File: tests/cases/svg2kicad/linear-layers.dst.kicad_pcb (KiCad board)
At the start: 2 copper layers, 0 parts

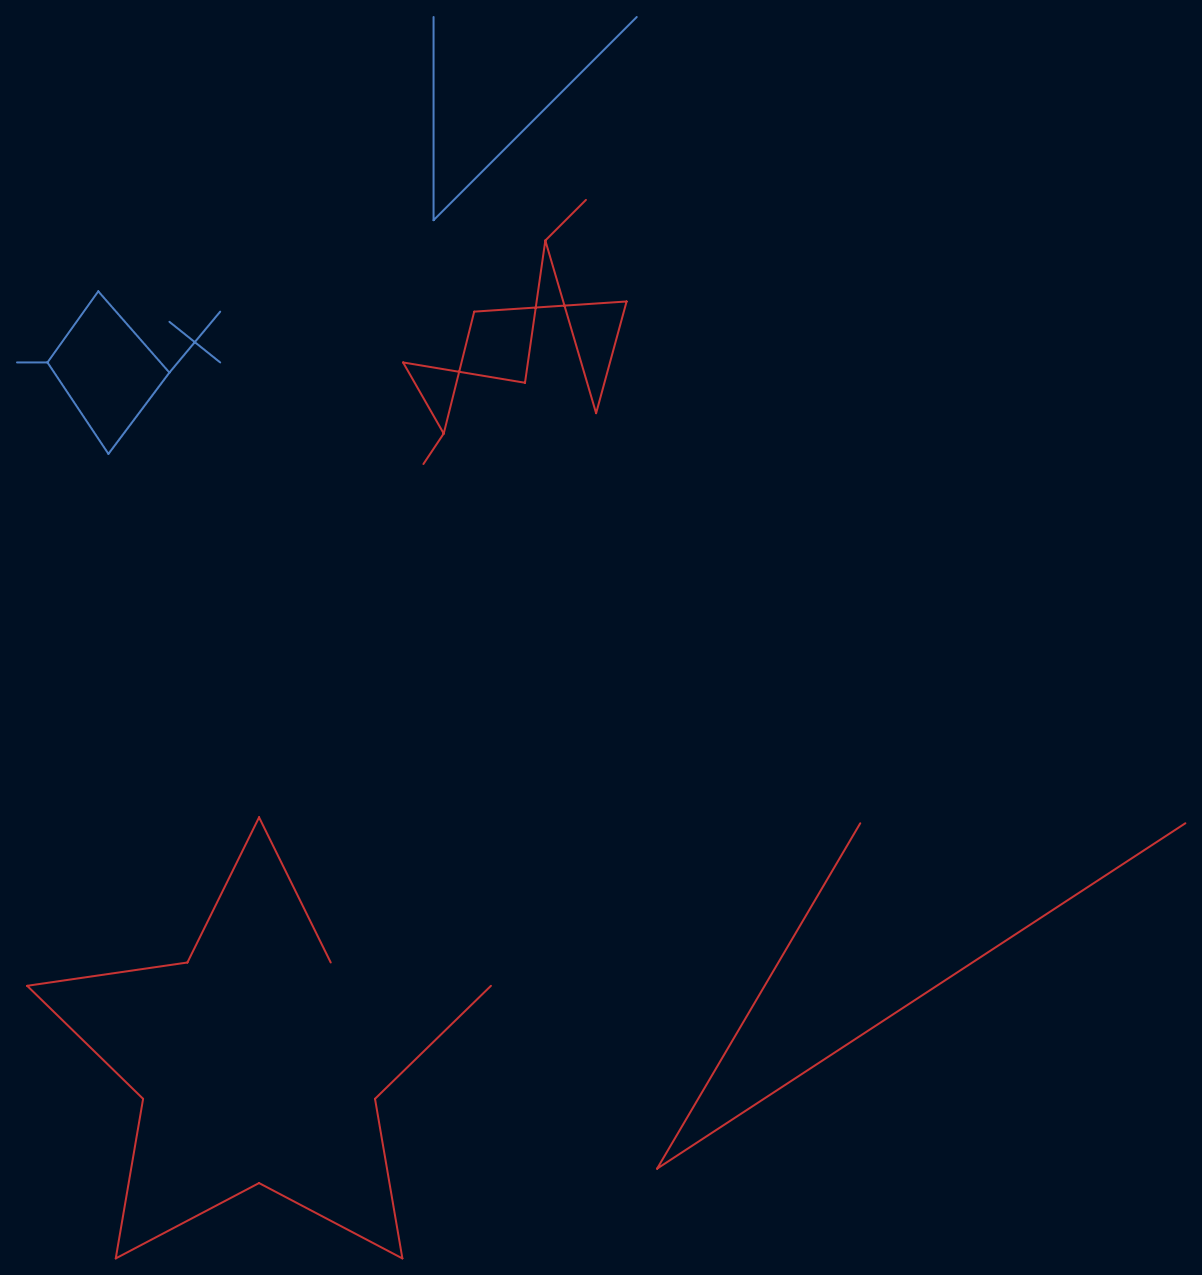
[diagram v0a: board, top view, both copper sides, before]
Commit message: Replace KiCad paths based on SVG layer names. Fix svg2kicad save in place. Add support for SVG path arc segments with equal radii. Add SVG path arc unit tests. Add SVG style function.
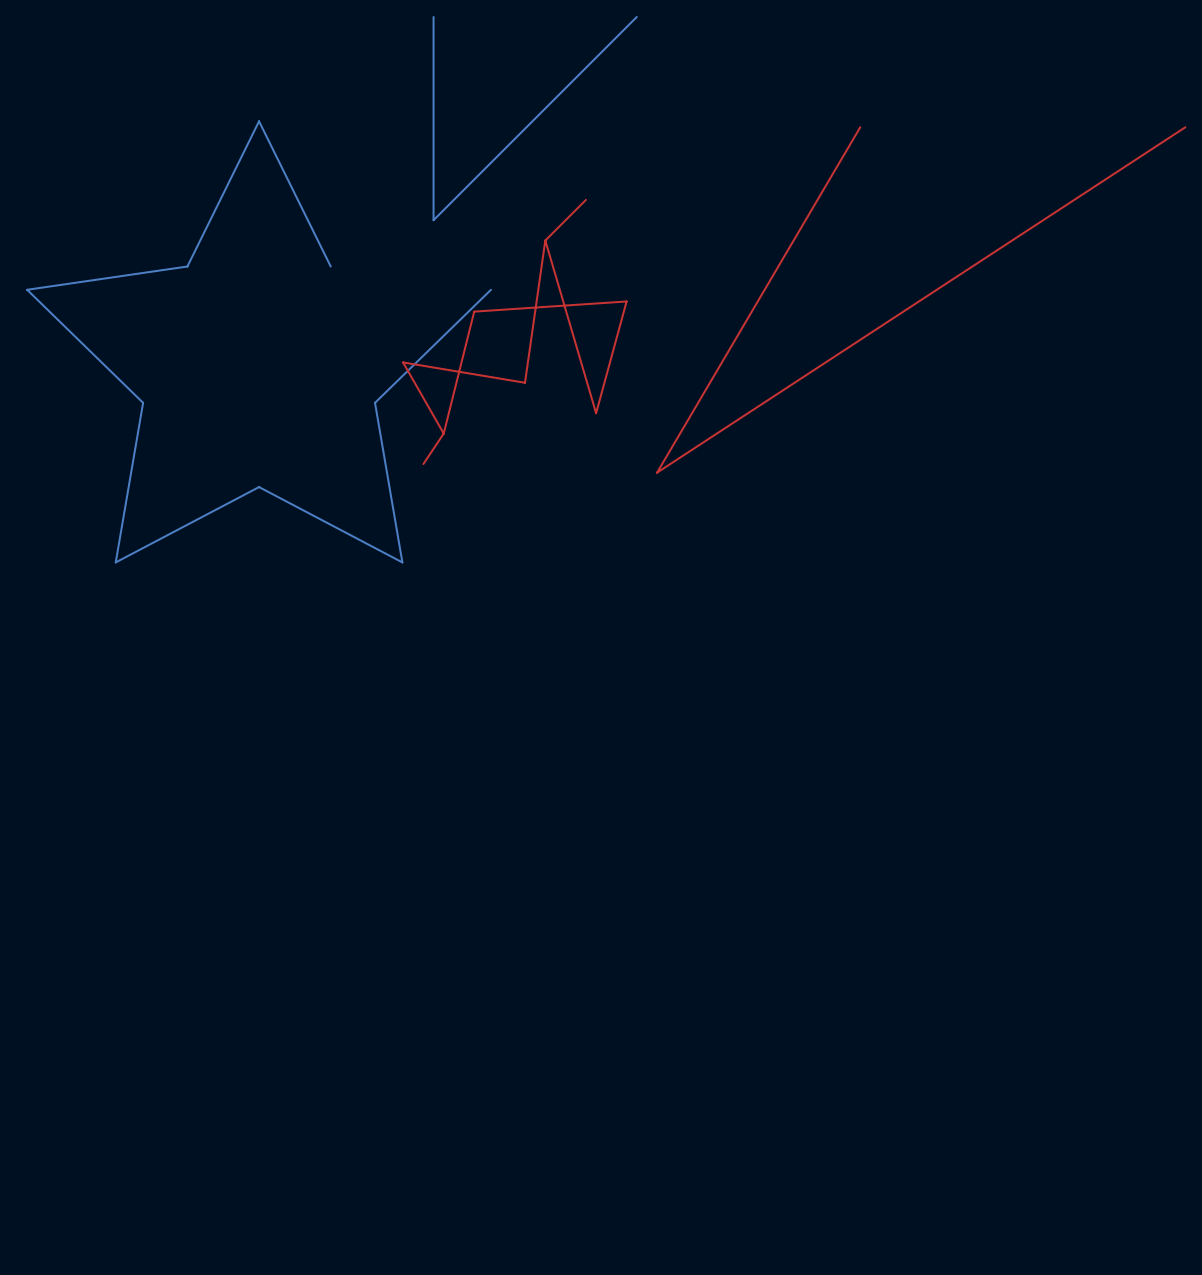
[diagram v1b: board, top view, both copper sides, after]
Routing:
- net (no net): track 372.5 -> 190.3 mm
- net Net-1: track 199.9 -> 309.4 mm
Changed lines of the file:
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@@
     (uvia_drill 0.1)
   )
-(segment (start 68.882 160.628) (end 83.376 146.500) (width 0.25) (layer F.Cu) (net 0))
-(segment (start 72.304 180.578) (end 68.882 160.628) (width 0.25) (layer F.Cu) (net 0))
-(segment (start 54.388 171.159) (end 72.304 180.578) (width 0.25) (layer F.Cu) (net 0))
-(segment (start 36.473 180.578) (end 54.388 171.159) (width 0.25) (layer F.Cu) (net 0))
-(segment (start 39.894 160.628) (end 36.473 180.578) (width 0.25) (layer F.Cu) (net 0))
-(segment (start 25.400 146.500) (end 39.894 160.628) (width 0.25) (layer F.Cu) (net 0))
-(segment (start 45.430 143.589) (end 25.400 146.500) (width 0.25) (layer F.Cu) (net 0))
-(segment (start 54.388 125.439) (end 45.430 143.589) (width 0.25) (layer F.Cu) (net 0))
-(segment (start 63.346 143.589) (end 54.388 125.439) (width 0.25) (layer F.Cu) (net 0))
-(segment (start 104.140 169.360) (end 129.540 126.180) (width 0.25) (layer F.Cu) (net 0))
-(segment (start 170.180 126.180) (end 104.140 169.360) (width 0.25) (layer F.Cu) (net 0))
+        (segment (start 68.882 73.628)         (end 83.376 59.500)         (width 0.25) (layer B.Cu) (net 1))
+        (segment (start 72.304 93.578)         (end 68.882 73.628)         (width 0.25) (layer B.Cu) (net 1))
+        (segment (start 54.388 84.159)         (end 72.304 93.578)         (width 0.25) (layer B.Cu) (net 1))
+        (segment (start 36.473 93.578)         (end 54.388 84.159)         (width 0.25) (layer B.Cu) (net 1))
+        (segment (start 39.894 73.628)         (end 36.473 93.578)         (width 0.25) (layer B.Cu) (net 1))
+        (segment (start 25.400 59.500)         (end 39.894 73.628)         (width 0.25) (layer B.Cu) (net 1))
+        (segment (start 45.430 56.589)         (end 25.400 59.500)         (width 0.25) (layer B.Cu) (net 1))
+        (segment (start 54.388 38.439)         (end 45.430 56.589)         (width 0.25) (layer B.Cu) (net 1))
+        (segment (start 63.346 56.589)         (end 54.388 38.439)         (width 0.25) (layer B.Cu) (net 1))
+        (segment (start 104.140 82.360)         (end 129.540 39.180)         (width 0.25) (layer F.Cu) (net 0))
+        (segment (start 170.180 39.180)         (end 104.140 82.360)         (width 0.25) (layer F.Cu) (net 0))
   (segment (start 76.2 25.4) (end 76.2 50.8) (width 0.25) (layer B.Cu) (net 0))
   (segment (start 76.2 50.8) (end 101.6 25.4) (width 0.25) (layer B.Cu) (net 0))
-  (segment (start 27.94 68.58) (end 34.29 59.69) (width 0.25) (layer B.Cu) (net 1))
-  (segment (start 34.29 59.69) (end 43.18 69.85) (width 0.25) (layer B.Cu) (net 1))
-  (segment (start 43.18 69.85) (end 35.56 80.01) (width 0.25) (layer B.Cu) (net 1))
-  (segment (start 35.56 80.01) (end 27.94 68.58) (width 0.25) (layer B.Cu) (net 1))
-  (segment (start 43.18 69.85) (end 49.53 62.23) (width 0.25) (layer B.Cu) (net 1))
-  (segment (start 43.18 63.5) (end 49.53 68.58) (width 0.25) (layer B.Cu) (net 1))
   (segment (start 77.47 77.47) (end 81.28 62.23) (width 0.25) (layer F.Cu) (net 1))
   (segment (start 81.28 62.23) (end 100.33 60.96) (width 0.25) (layer F.Cu) (net 1))
@@
   (segment (start 77.47 77.47) (end 74.93 81.28) (width 0.25) (layer F.Cu) (net 1))
   (segment (start 90.17 53.34) (end 95.25 48.26) (width 0.25) (layer F.Cu) (net 1))
-  (segment (start 27.94 68.58) (end 24.13 68.58) (width 0.25) (layer B.Cu) (net 1))
 )
